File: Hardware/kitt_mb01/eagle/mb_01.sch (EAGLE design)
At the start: 90 parts, among them CON1 ARDUINO_UNO, IC1.01 RT8293A, IC2.00 BQ24266RGET, IC3.01 LSM9DS1, P1 JST.S2B-PH-SM4-TB, U1 TPS61032RSARPSDO-G16

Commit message: moved merged layout to main directory and deleted garbage
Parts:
- removed CON1: ARDUINO_UNO, kitt.con:ARDUINO_UNO
- removed D1: MBRS320T3, diode:MBRS320T3
- removed F1: 750mA, fuse:MF-SMDF050
- removed IC1: (no value), kitt.ic:DRV8871
- removed L1.01, L4.01: BEAD, inductors:BLM15HB121SN1
- removed L2.02: BEAD, rcl:L-EUL2012C
- removed P1: JST.S2B-PH-SM4-TB, kitt.con:JST.S2B-PH-SM4-TB
- removed R2: 10kR, rcl:R-EU_M0805
- removed R2.06: 10kR/NTC, ptc-ntc:V642
- removed R3: 2k2R, rcl:R-EU_M0805
- removed R4.01, R4.02: [0R], rcl:R-EU_M0805
- removed RAILS, SOC, SOC1: (no value), con-phoenix-254:MPT2
- removed SJ1: (no value), jumper:SJ
- removed U1: TPS61032RSARPSDO-G16, kitt.ic:TPS61032RSARPSDO-G16
- added D1.01: MBRS320T3, diode:MBRS320T3
- added D7.03, D7.04: (no value), led:LEDCHIPLED_1206
- added D7.05: OK+5V, led:LEDCHIPLED_1206
- added D7.06: OK+3V, led:LEDCHIPLED_1206
- added D7.07: OK+12V, led:LEDCHIPLED_1206
- added F1.01: 750mA, rcl:R-EU_R1210
- added FB1.01, FB1.02, FB2.01, FB4.01: BEAD, rcl:L-EUL4516C
- added IC4.01: (no value), kitt.ic:DRV8871
- added J4.01: (no value), jumper:SJ2W
- added NTC+, NTC-: (no value), wirepad:SMD2
- added R7,01, R7,02, R7,04, R7,05, R7.01, R7.04, R7.08, R7.10: 330R, rcl:R-EU_R0603
- added R7.02: 10kR, rcl:R-EU_M0805
- added R7.03: 2k2R, rcl:R-EU_M0805
- added R7.05, R7.06, R7.07: [0R], jumper:SJ
- added R7.09: [0R], rcl:R-EU_R0603
- added R7.11, R7.12: SHUNT, rcl:R-EU_R1206
- added REF2: REF.LOGO.UASUA, kitt.refs:REF.LOGO.UASUA
- added U6.01: TPS61032RSARPSDO-G16, kitt.ic:TPS61032RSARPSDO-G16
- added U7.01, U7.03, U7.2: SI1922EDH, kitt.ic:SI1922EDH
- added X2.01: S2B-PH-K-S(LF)(SN), kitt.con:S2B-PH-K-S(LF)(SN)
- added X7.01, X7.04: (no value), con-phoenix-254:MPT2
- added X7.02: ARDUINO_UNO, kitt.con:ARDUINO_UNO
- added X7.03, X7.06, X7.08, X7.11: CON_HEADER_1X02, kitt.con:CON_HEADER_1X02
- added X7.05: MOTOR, con-phoenix-254:MPT2
- added X7.07: (no value), pinhead:PINHD-2X3/90
- added X7.09, X7.10: 0R-JUMPA, jump-0r-smd:0R-JUMPA
- C1.04: value XX -> 3.3nF
- C3.01: device rcl:C-EUC0402 -> rcl:C-EUC0603
- C3.03, C3.05: value 10nF -> 100nF
- C3.04: device rcl:C-EUC0603K -> resistor:C-EUC0603K
- C4.03: value (none) -> 4.7uF
- FB6.01: device inductors:BLM15HB121SN1 -> rcl:L-EUL4516C
- L1.02: value 4.7uH -> 15uH; device rcl:L-EUWE-TPC -> kitt.psvs:NRS8030XX
- L2: value BEAD -> (none); device inductors:BLM15HB121SN1 -> rcl:L-EUL4516C
- L2.01: device rcl:L-EUWE-TPC -> kitt.psvs:NRS8030XX
- R1.02: value XX -> 20kR
- R1.03: value XX -> 62kR
- R1.04: value XX -> 11.8kR
- renumbered Q1 to Q2.01
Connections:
- new net ARDUINO.SCL: IC3.01.SCL/SPC
- new net ARDUINO.SDA: IC3.01.SDA/SDI/SDO
- new net CAR.AUXILLARY: U7.2A.G, X7.02G$4.IO.10
- new net CAR.BLIGHT: U7.2B.G, X7.02G$3.IO.5
- new net CAR.FLIGHT: U7.01A.G, X7.02G$3.IO.6
- new net CAR.GATECTLR: U7.01B.G, X7.02G$4.IO.9
- new net CAR.LAPCNT: X7.02G$3.IO.7, X7.07.1
- new net CAR.SPEED: X7.02G$4.IO.8, X7.07.2
- new net N$25: R7.11.1, X7.04-2.1
- new net N$28: D7.03.C, U7.03A.D
- new net N$30: D7.04.A, R7.01.1
- new net N$31: D7.04.C, U7.03B.D
- new net N$38: D7.06.A, R7,04.1
- new net N$4: R7.06.2, X7.02G$2.5V
- new net N$42: R7.04.2, X7.08.1
- new net N$44: D7.07.A, R7,05.1
- new net N$45: X7.08.2, X7.10-0R.2, X7.11.1
- new net N$46: R7.09.2, X7.06.1
- new net N$47: R7.09.1, U7.2B.D
- new net N$48: X7.03.1, X7.06.2, X7.09-0R.2
- new net N$5: R7.07.2, X7.02G$2.VIN
- new net N$50: R7.08.2, X7.11.2
- new net N$51: R7.10.1, U7.2A.D
- new net N$52: R7.10.2, X7.03.2
- new net N$7: R7.08.1, U7.01B.D
- new net N$80: F1.01.2, FB1.01.1
- new net N$81: C1.01.1, FB1.01.2, IC1.01.VIN, R1.01.1
- new net N$87: C1.05.1, C1.06.1, FB1.02.1, L1.02.1, R1.03.2
- new net N$90: FB1.02.2, R1.05.2, R1.06.1
- net !IRQ_GYRO: now also X7.02G$3.IO.2; no longer CON1G$3.IO.2
- net +12V: now also D1.01.C, F1.01.1, FB4.01.2, R7,05.2, R7.02.1, R7.07.1; no longer D1.C, F1.1, L4.01.2, R2.1
- net +3V3: now also R7,01.2, R7,04.2, R7.01.2, R7.05.1, X7.07.5, X7.07.6, X7.09-0R.1, X7.10-0R.1
- net +4.1V: now also U6.01.VBAT, X2.01.1; no longer P1.1, U1.VBAT
- net +5V: now also R7,02.2, R7.06.1, X7.04-1.1, X7.09-0R.3, X7.10-0R.3; no longer SOC-1.1
- net GND: now also C6.02.2, D7.05.C, D7.06.C, D7.07.C, IC4.01.GND, IC4.01.PAD, IC4.01.PGND, J4.01.1, NTC-.P, R7.03.2, R7.11.2, R7.12.2, U6.01.EP, U6.01.GND, U6.01.PGND, U6.01.PGND_2, U6.01.PGND_3, U7.01A.S, U7.01B.S, U7.03A.S, U7.03B.S, U7.2A.S, U7.2B.S, X2.01.2, X7.02G$2.GND@1, X7.02G$2.GND@2, X7.07.3, X7.07.4; no longer CON1G$2.GND@1, CON1G$2.GND@2, IC1.GND, IC1.PAD, IC1.PGND, P1.2, R2.06.1, R3.2, R4.01.1, SJ1.2, SOC-2.1, U1.EP, U1.GND, U1.PGND_3
- net GNDA: now also R7.12.1, X7.01-1.1; no longer RAILS-2.1, SJ1.1
- net IC2.0.!CHG: now also U7.03A.G
- net IC2.0.!PG: now also U7.03B.G
- net LBO: now also U6.01.LBO, X7.02G$1.ADC.0; no longer CON1G$1.ADC.0, U1.LBO
- net MOT.IN1: now also IC4.01.IN1, X7.02G$3.IO.3; no longer CON1G$3.IO.3, IC1.IN1
- net MOT.IN2: now also IC4.01.IN2, X7.02G$3.IO.4; no longer CON1G$3.IO.4, IC1.IN2
- net N$10: now also FB4.01.1, IC4.01.VM; no longer IC1.VM, L4.01.1
- net N$15: now also NTC+.P; no longer R2.06.2
- net N$16: now also FB2.01.2; no longer L2.02.2
- net N$18: now also FB2.01.1; no longer L2.02.1
- net N$2: now also R7.04.1, U7.01A.D; no longer F1.2, L1.01.1
- net N$29: now also D7.03.A, R7,01.1; no longer C1.05.1, C1.06.1, L1.02.1, L2.1, R1.03.2
- net N$3: now also R7.05.2, X7.02G$2.3V3; no longer C1.01.1, IC1.01.VIN, L1.01.2, R1.01.1
- net N$32: now also D7.05.A, R7,02.1; no longer L2.2, R1.05.2, R1.06.1
- net N$33: now also IC4.01.OUT1, X7.05-1.1; no longer IC1.OUT1, SOC1-1.1
- net N$34: now also IC4.01.OUT2, J4.01.3; no longer IC1.OUT2, R4.02.2
- net N$35: now also IC4.01.ILIM; no longer IC1.ILIM
- net N$37: now also U6.01.EN; no longer U1.EN
- net N$39: now also U6.01.SW, U6.01.SW_2; no longer U1.SW, U1.SW_2
- net N$40: now also U6.01.LBI; no longer U1.LBI
- net N$41: now also U6.01.SYNC; no longer U1.SYNC
- net N$43: now also U6.01.VOUT, U6.01.VOUT_2, U6.01.VOUT_3; no longer U1.VOUT, U1.VOUT_2, U1.VOUT_3
- net N$9: now also J4.01.2, X7.05-2.1; no longer R4.01.2, R4.02.1, SOC1-2.1
- net RAILS.RX: now also R7.02.2, R7.03.1, X7.02G$3.IO.0; no longer CON1G$3.IO.0, R2.2, R3.1
- net SCL: now also X7.02G$4.SCL; no longer CON1G$4.SCL
- net SDA: now also X7.02G$4.SDA; no longer CON1G$4.SDA
- net VCC/2: now also D1.01.A, X7.01-2.1; no longer D1.A, RAILS-1.1
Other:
- note added: "D.Hoeglinger/A.Gessler"
- note added: "KITT MB01 - 5V Rail Power"
- note added: "KITT MB01 - Full Bridge Driver"
- note added: "TODO"

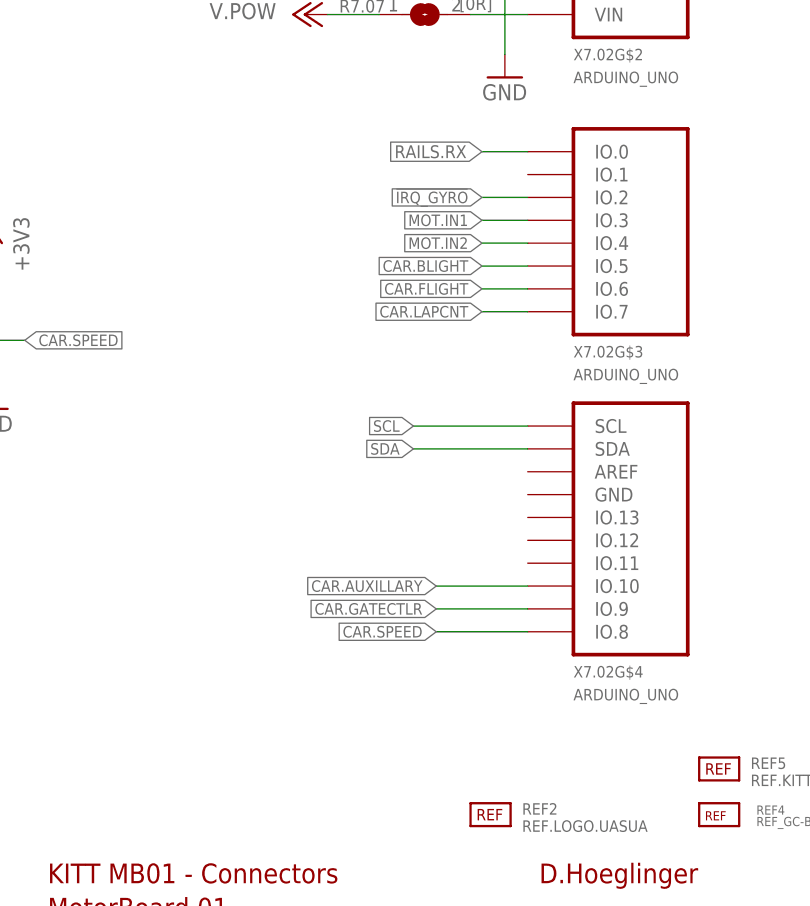
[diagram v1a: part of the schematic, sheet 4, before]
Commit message: snapshot of mb-01 board -> double-checked pin usage between pcbs, needed to reroute one signal
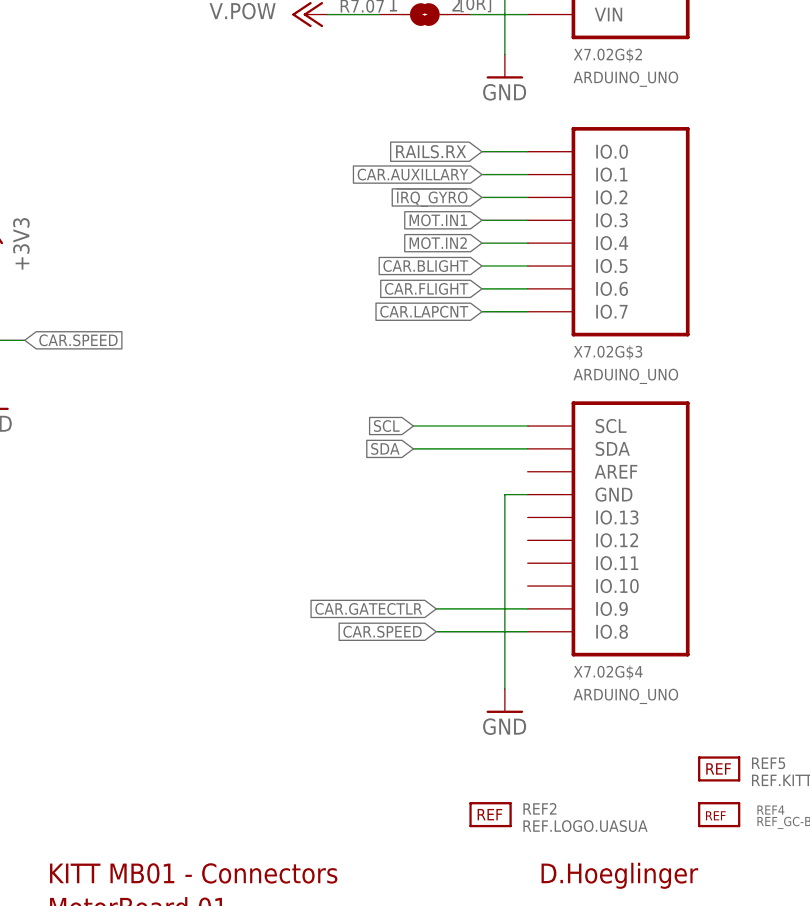
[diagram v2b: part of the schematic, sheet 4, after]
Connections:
- net CAR.AUXILLARY: now also X7.02G$3.IO.1; no longer X7.02G$4.IO.10
- net GND: now also X7.02G$4.GND
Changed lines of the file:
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@@
 <setting verticaltext="up"/>
 </settings>
-<grid distance="0.025" unitdist="inch" unit="inch" style="lines" multiple="1" display="no" altdistance="0.01" altunitdist="inch" altunit="inch"/>
+<grid distance="0.05" unitdist="inch" unit="inch" style="lines" multiple="1" display="no" altdistance="0.01" altunitdist="inch" altunit="inch"/>
 <layers>
 <layer number="1" name="Top" color="4" fill="1" visible="no" active="no"/>
@@
 <part name="R7.10" library="rcl" deviceset="R-EU_" device="R0603" value="330R"/>
 <part name="L2" library="rcl" deviceset="L-EU" device="L4516C"/>
+<part name="GND27" library="supply1" deviceset="GND" device=""/>
 </parts>
 <sheets>
@@
 <instance part="X7.03" gate="G$1" x="66.04" y="55.88"/>
 <instance part="R7.10" gate="G$1" x="46.355" y="43.18" rot="R90"/>
+<instance part="GND27" gate="1" x="213.36" y="39.37"/>
 </instances>
 <busses>
@@
 <wire x1="55.245" y1="71.12" x2="55.245" y2="73.66" width="0.1524" layer="91"/>
 </segment>
+<segment>
+<pinref part="GND27" gate="1" pin="GND"/>
+<pinref part="X7.02" gate="G$4" pin="GND"/>
+<wire x1="213.36" y1="41.91" x2="213.36" y2="63.5" width="0.1524" layer="91"/>
+<wire x1="213.36" y1="63.5" x2="215.9" y2="63.5" width="0.1524" layer="91"/>
+</segment>
 </net>
 <net name="RAILS.RX" class="0">
@@
 </segment>
 <segment>
-<wire x1="205.74" y1="53.34" x2="215.9" y2="53.34" width="0.1524" layer="91"/>
-<label x="205.74" y="53.34" size="1.27" layer="95" rot="R180" xref="yes"/>
-<pinref part="X7.02" gate="G$4" pin="IO.10"/>
-</segment>
-</net>
+<label x="210.82" y="99.06" size="1.27" layer="95" rot="R180" xref="yes"/>
+<pinref part="X7.02" gate="G$3" pin="IO.1"/>
+<wire x1="210.82" y1="99.06" x2="215.9" y2="99.06" width="0.1524" layer="91"/>
+</segment>
+</net>

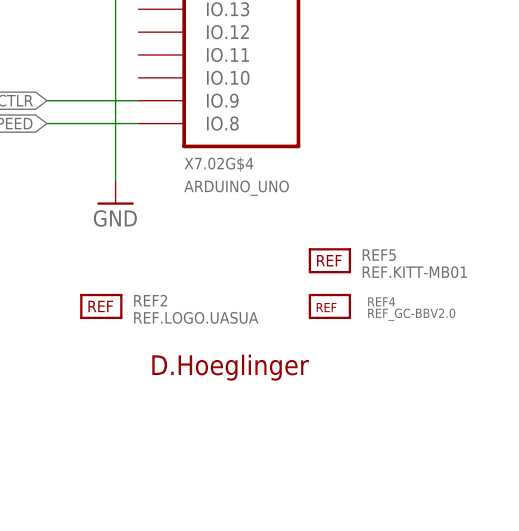
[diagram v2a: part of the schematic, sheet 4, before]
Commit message: snapshot of mb01 board layout -> rearranged some vias -> minor reroutes were done -> started working on top silk layer
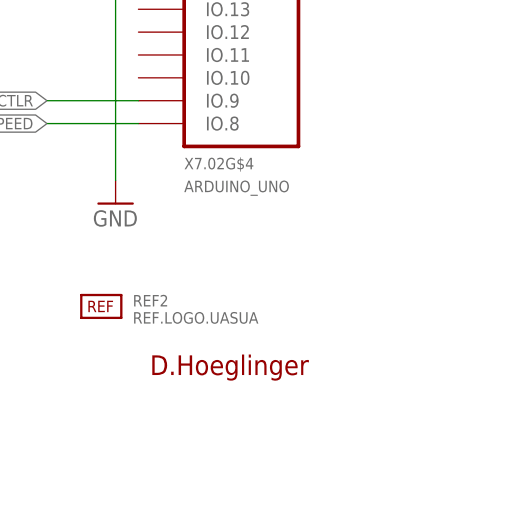
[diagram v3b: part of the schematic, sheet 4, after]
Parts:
- removed L2: (no value), rcl:L-EUL4516C
- removed REF4: REF_GC-BBV2.0, kitt.con:REF_GC-BBV2.0
- removed REF5: REF.KITT-MB01, kitt.refs:REF.KITT-MB01
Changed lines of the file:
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@@
 <setting verticaltext="up"/>
 </settings>
-<grid distance="0.05" unitdist="inch" unit="inch" style="lines" multiple="1" display="no" altdistance="0.01" altunitdist="inch" altunit="inch"/>
+<grid distance="0.1" unitdist="inch" unit="inch" style="lines" multiple="1" display="no" altdistance="0.01" altunitdist="inch" altunit="inch"/>
 <layers>
 <layer number="1" name="Top" color="4" fill="1" visible="no" active="no"/>
@@
 <part name="FRAME3" library="frames" deviceset="A4L-LOC" device=""/>
 <part name="X7.02" library="kitt.con" deviceset="ARDUINO_UNO" device=""/>
-<part name="REF4" library="kitt.con" deviceset="REF_GC-BBV2.0" device=""/>
 <part name="GND7" library="supply1" deviceset="GND" device=""/>
 <part name="R7.02" library="rcl" deviceset="R-EU_" device="M0805" value="10kR"/>
 <part name="R7.03" library="rcl" deviceset="R-EU_" device="M0805" value="2k2R"/>
 <part name="GND8" library="supply1" deviceset="GND" device=""/>
-<part name="REF5" library="kitt.refs" deviceset="REF.KITT-MB01" device=""/>
 <part name="P+5VMAIN1" library="supply1" deviceset="+5V" device="" value="+5V-MAIN"/>
 <part name="X7.04" library="con-phoenix-254" deviceset="MPT2" device=""/>
@@
 <part name="X7.03" library="kitt.con" deviceset="CON_HEADER_1X02" device=""/>
 <part name="R7.10" library="rcl" deviceset="R-EU_" device="R0603" value="330R"/>
-<part name="L2" library="rcl" deviceset="L-EU" device="L4516C"/>
 <part name="GND27" library="supply1" deviceset="GND" device=""/>
 </parts>
@@
 <instance part="X7.02" gate="G$3" x="223.52" y="91.44"/>
 <instance part="X7.02" gate="G$4" x="226.06" y="58.42"/>
-<instance part="REF4" gate="G$1" x="234.95" y="26.67"/>
 <instance part="GND7" gate="1" x="213.36" y="109.855"/>
 <instance part="R7.02" gate="G$1" x="139.065" y="50.8" rot="MR270"/>
 <instance part="R7.03" gate="G$1" x="139.065" y="35.56" rot="MR270"/>
 <instance part="GND8" gate="1" x="139.065" y="25.4"/>
-<instance part="REF5" gate="G$1" x="234.95" y="31.75"/>
 <instance part="P+5VMAIN1" gate="1" x="27.94" y="167.64" rot="MR0"/>
 <instance part="X7.04" gate="-1" x="20.32" y="160.02" rot="MR0"/>
@@
 <instance part="R4.05" gate="G$1" x="99.06" y="73.66" rot="R90"/>
 <instance part="J4.01" gate="G$1" x="193.04" y="81.28" rot="R180"/>
-<instance part="L2" gate="G$1" x="218.44" y="62.23"/>
 </instances>
 <busses>

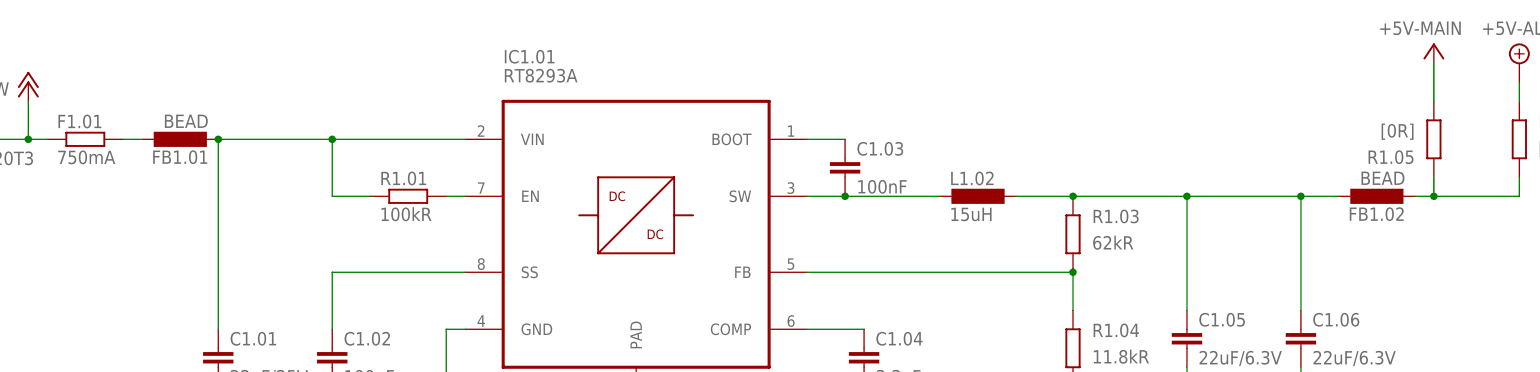
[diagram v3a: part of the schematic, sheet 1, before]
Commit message: snapshot of mb01 board layout -> did majority of top silk names, values have been deleted    because there's not enough time for such things
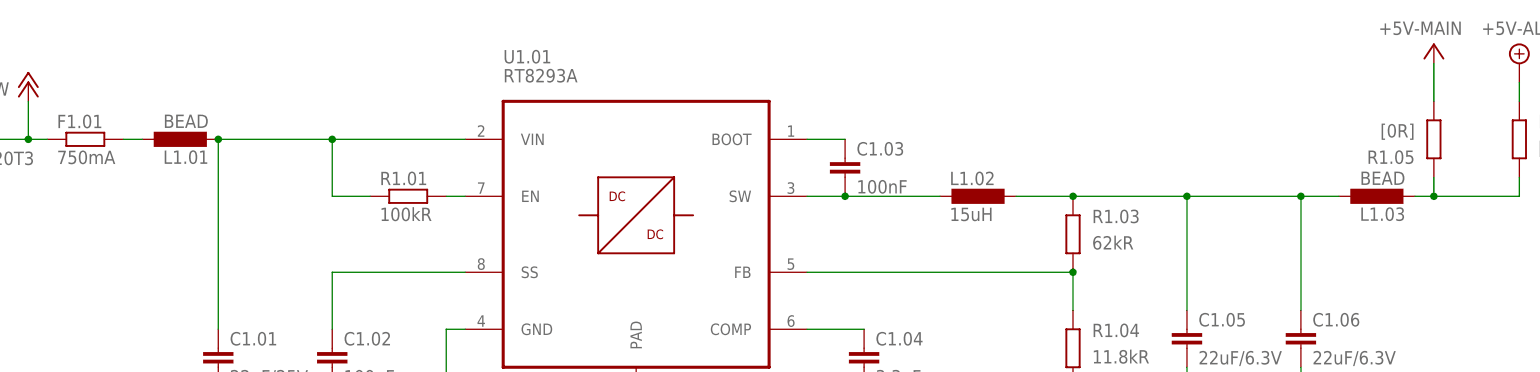
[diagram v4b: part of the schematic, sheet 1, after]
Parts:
- renumbered FB1.01 to L1.01, FB1.02 to L1.03, FB4.01 to L4.01, FB6.01 to L6.02, IC1.01 to U1.01, IC4.01 to U4.01

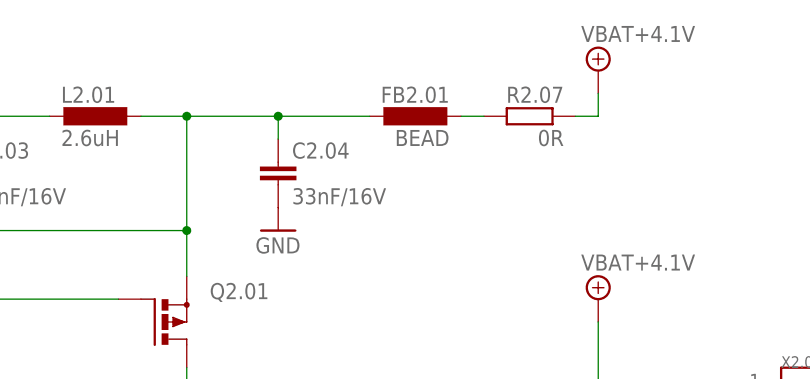
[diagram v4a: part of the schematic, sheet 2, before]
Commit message: snapshot of mb01 board layout -> forgot a DRC check for the silk layer -> fixed all overlaps for top silk
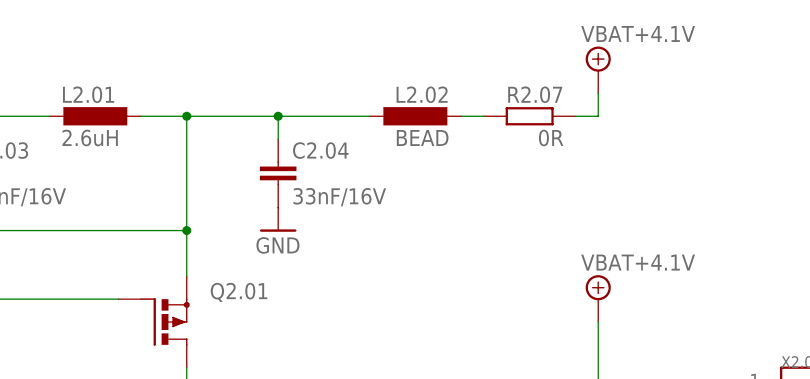
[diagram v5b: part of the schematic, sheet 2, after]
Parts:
- renumbered FB2.01 to L2.02
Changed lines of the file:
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@@
 <part name="C2.04" library="rcl" deviceset="C-EU" device="C0805" value="33nF/16V"/>
 <part name="GND13" library="supply1" deviceset="GND" device=""/>
-<part name="FB2.01" library="rcl" deviceset="L-EU" device="L4516C" value="BEAD"/>
+<part name="L2.02" library="rcl" deviceset="L-EU" device="L4516C" value="BEAD"/>
 <part name="R2.07" library="rcl" deviceset="R-EU_" device="R0402" value="0R"/>
 <part name="GND14" library="supply1" deviceset="GND" device=""/>
@@
 <instance part="C2.04" gate="G$1" x="160.02" y="139.7"/>
 <instance part="GND13" gate="1" x="160.02" y="132.08"/>
-<instance part="FB2.01" gate="G$1" x="175.26" y="144.78" rot="MR270"/>
+<instance part="L2.02" gate="G$1" x="175.26" y="144.78" rot="MR270"/>
 <instance part="R2.07" gate="G$1" x="187.96" y="144.78" rot="MR0"/>
 <instance part="GND14" gate="1" x="132.08" y="99.06" rot="R90"/>
@@
 <wire x1="160.02" y1="144.78" x2="160.02" y2="142.24" width="0.1524" layer="91"/>
 <junction x="149.86" y="144.78"/>
-<pinref part="FB2.01" gate="G$1" pin="1"/>
+<pinref part="L2.02" gate="G$1" pin="1"/>
 <wire x1="170.18" y1="144.78" x2="160.02" y2="144.78" width="0.1524" layer="91"/>
 <junction x="160.02" y="144.78"/>
@@
 <net name="N$16" class="0">
 <segment>
-<pinref part="FB2.01" gate="G$1" pin="2"/>
+<pinref part="L2.02" gate="G$1" pin="2"/>
 <pinref part="R2.07" gate="G$1" pin="2"/>
 <wire x1="180.34" y1="144.78" x2="182.88" y2="144.78" width="0.1524" layer="91"/>

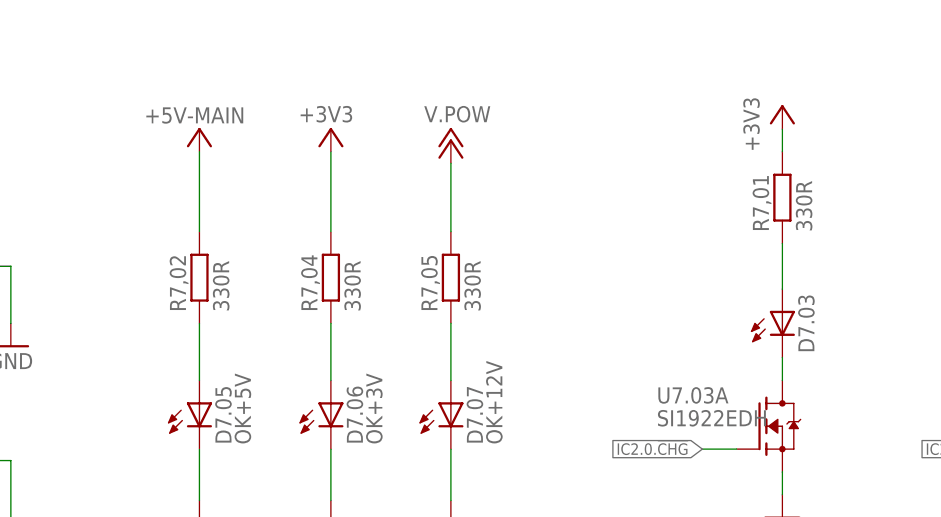
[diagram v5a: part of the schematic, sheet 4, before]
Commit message: snapshot of mb01 board layout : finishing touches edition -> finished all placement, signal routing and component label silkscreen -> next up is maximization of power routes at layer 2 and -> ground pours on top and bottom with sufficient ground stitching
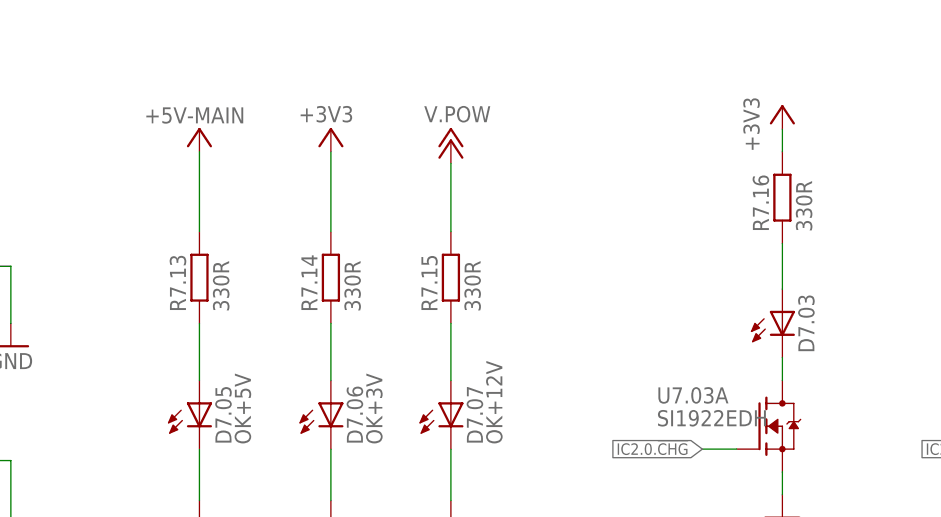
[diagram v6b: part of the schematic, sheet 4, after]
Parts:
- renumbered IC2.00 to IC2.0, R7,01 to R7.16, R7,02 to R7.13, R7,04 to R7.14, R7,05 to R7.15
